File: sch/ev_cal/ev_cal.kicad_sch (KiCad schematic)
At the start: 48 parts, among them J1 JTAG, J11 Conn_01x01_Male, J2 PROG, J3 Conn_01x04_Male, J4 Conn_01x04_Male, J5 Conn_01x04_Male, J6 Conn_01x04_Male, P1 Conn_WallPlug, SW1 SW_Push, SW2 SW_DIP_x02, U1 ESP32-WROOM-32E-N8, U10 LMV358, U11 ADM1085AKSZ-REEL7, U2 DC/DC - 5V, U3 DC/DC - 3.3V, U4 R503, U5 HW-111, U6 74HC595

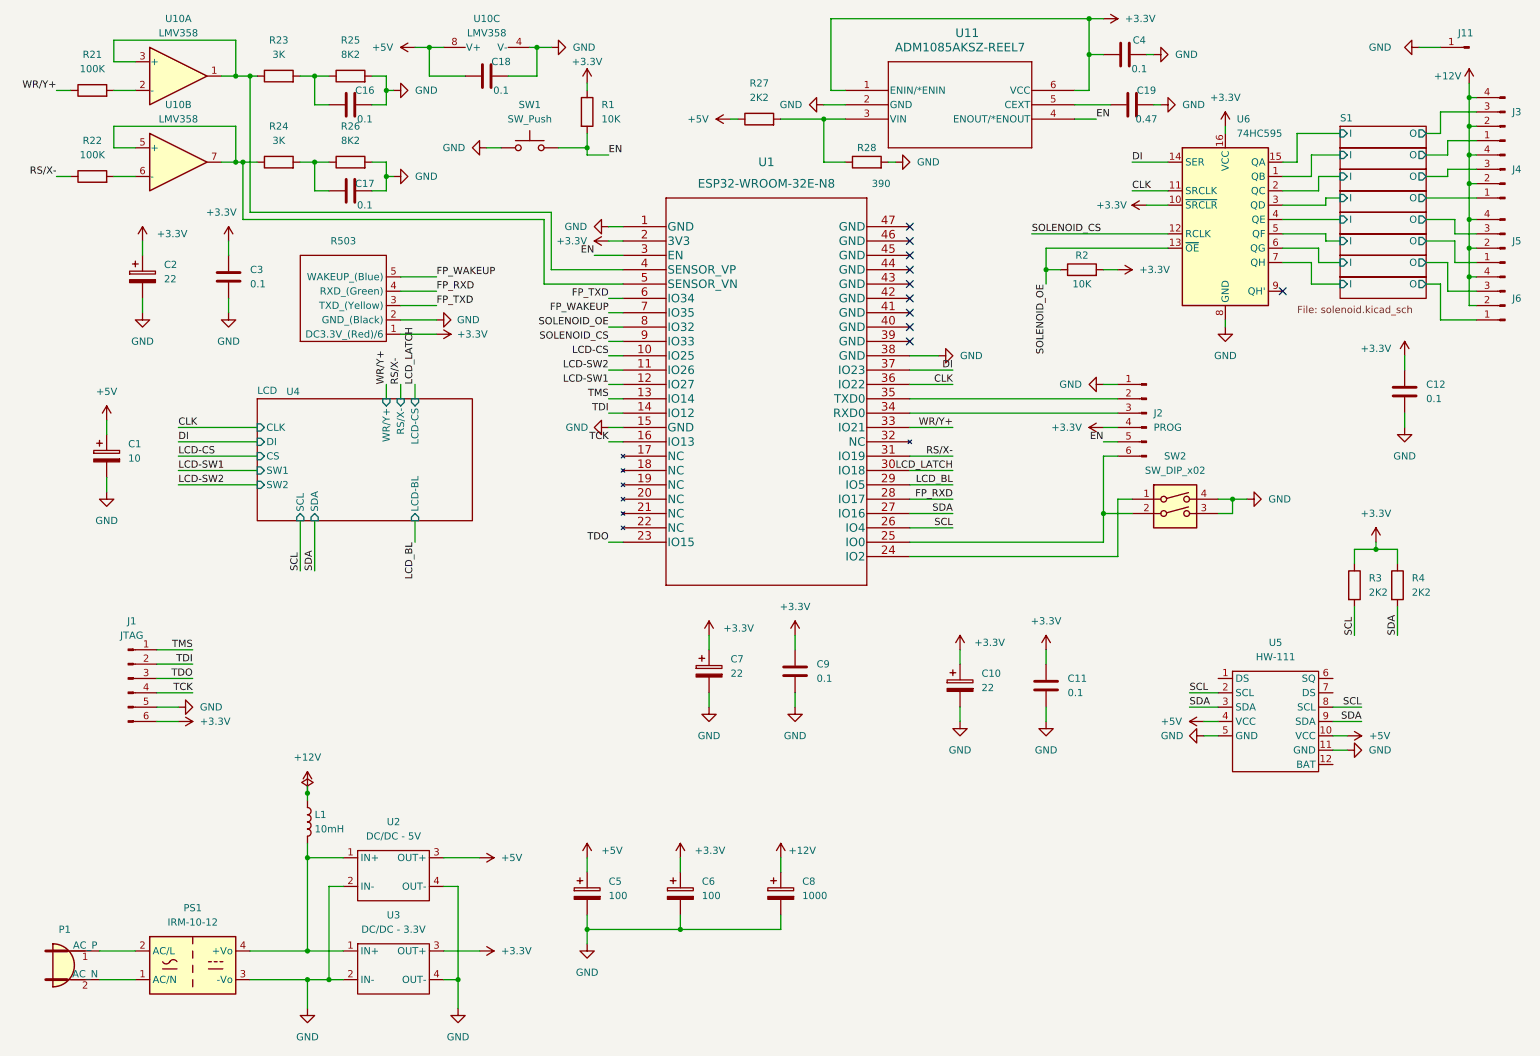
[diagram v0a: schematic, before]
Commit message: Added PDF of schematic
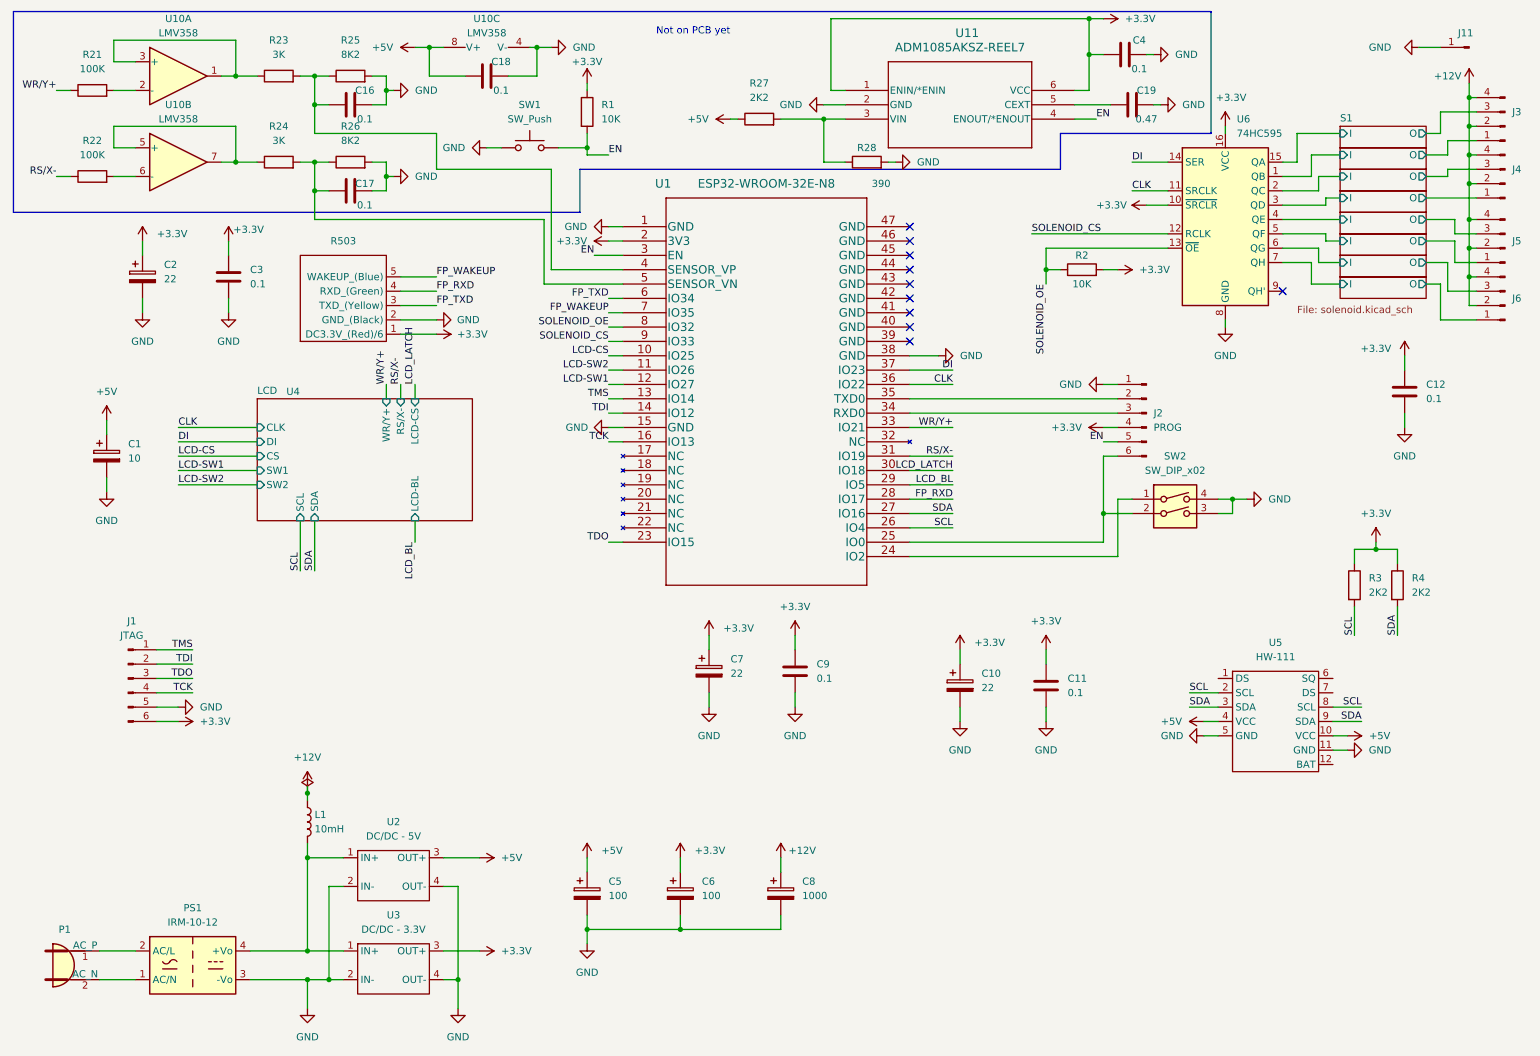
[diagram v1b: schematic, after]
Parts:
- U2, U3: symbol local:DC/DC -> local:DC/DC
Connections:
- net at C17.1, R24.2, R26.1: now also U1.5 (SENSOR_VN)
- net at R24.1, U10.5 (+), U10.7: no longer U1.5 (SENSOR_VN)
- net at C16.1, R23.2, R25.1: now also U1.4 (SENSOR_VP)
- net at R23.1, U10.1, U10.3 (+): no longer U1.4 (SENSOR_VP)
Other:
- note added: "Not on PCB yet"
